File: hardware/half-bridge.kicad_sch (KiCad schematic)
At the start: 9 parts, among them Q3 PSMN039-100YS, Q4 PSMN039-100YS, U6 LM2104D

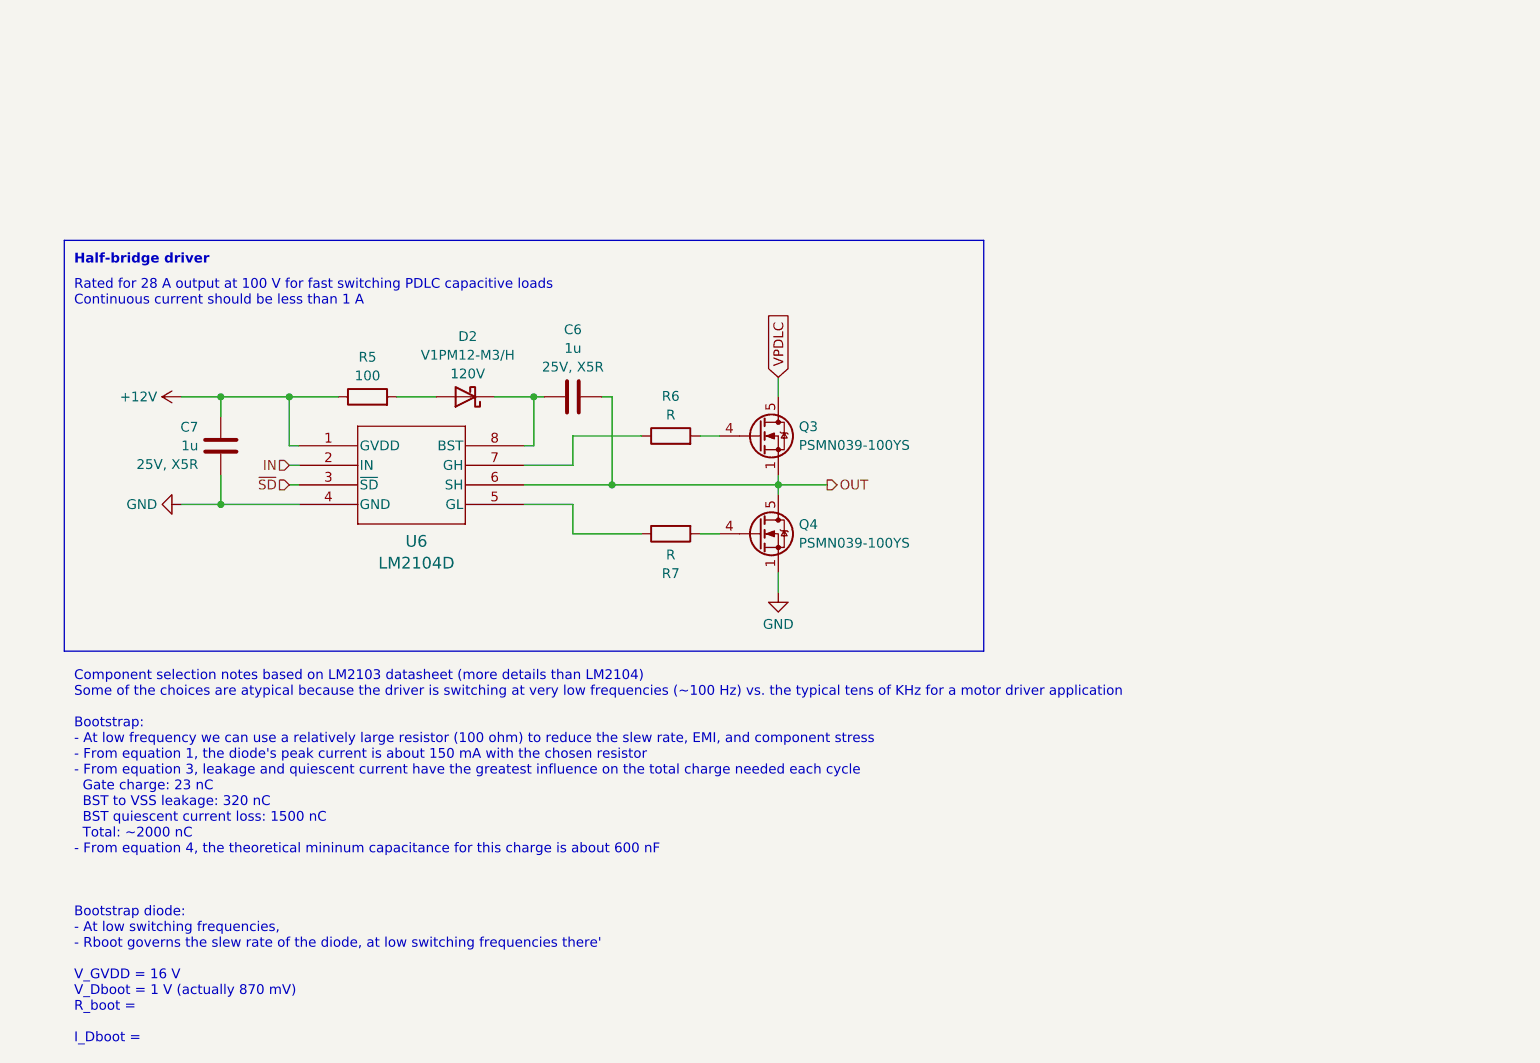
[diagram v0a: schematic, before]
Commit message: Revised layout using LM5108 and discrete FETs
LM5108 is less expensive but it requires more board area.  In lieu of
active current limiting, we rely on the LM5158 hiccup overload
protection.  The FETs are intentionally oversized to handle large
current pulses when switching the polarity of the capacitive load.

This design is complete and ready for manufacture.
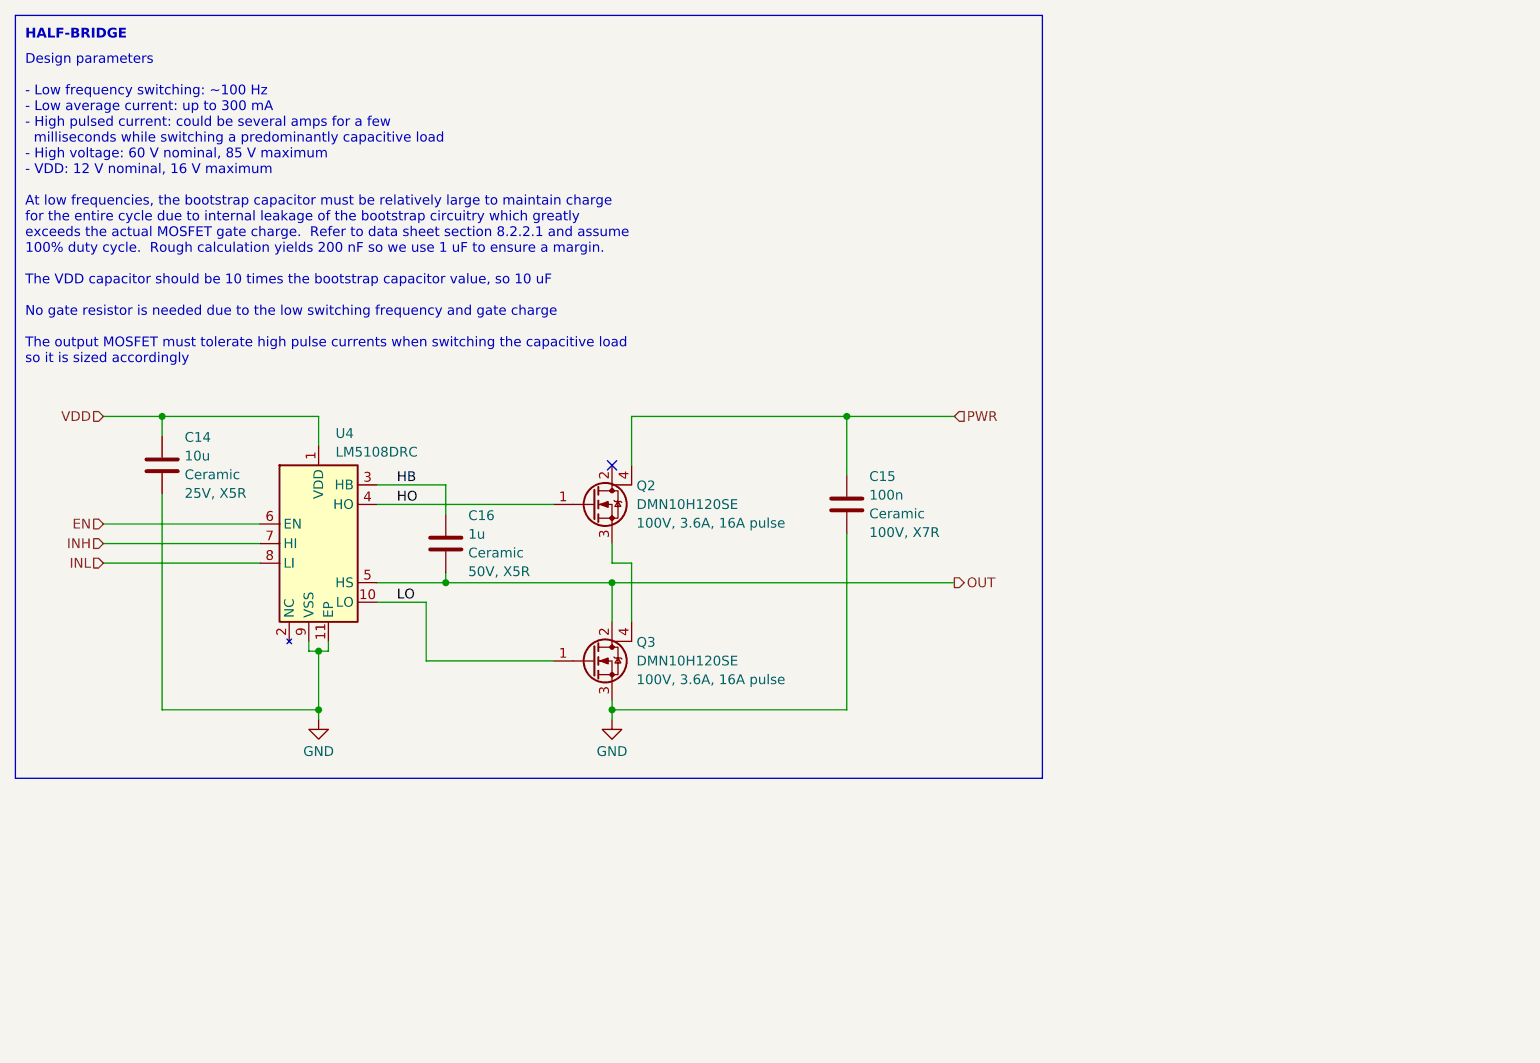
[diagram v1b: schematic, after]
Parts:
- removed C6: 1u, symbol Device:C
- removed C7: 1u, Capacitor_SMD:C_0603_1608Metric, symbol Device:C
- removed D2: V1PM12-M3/H, symbol Device:D_Schottky
- removed Q3, Q4: PSMN039-100YS, Package_TO_SOT_SMD:LFPAK56, symbol Transistor_FET:PSMN5R2-60YL
- removed R5: 100, symbol Device:R
- removed R6, R7: R, symbol Device:R
- removed U6: LM2104D, Package_SO:SOIC-8_3.9x4.9mm_P1.27mm, symbol LM2104D:LM2104D
- added C14: 10u, Capacitor_SMD:C_0603_1608Metric, symbol Device:C
- added C15: 100n, Capacitor_SMD:C_0805_2012Metric, symbol Device:C
- added C16: 1u, Capacitor_SMD:C_0603_1608Metric, symbol Device:C
- added Q2, Q3: DMN10H120SE, Package_TO_SOT_SMD:SOT-223, symbol Device:Q_NMOS_GDSD
- added U4: LM5108DRC, Package_SON:VSON-10-1EP_3x3mm_P0.5mm_EP1.65x2.4mm, symbol LM5108:LM5108DRC
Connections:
- net GND: now also C14.2, C15.2, Q3.3 (S), U4.11 (EP), U4.9 (VSS)
- net OUT: now also C16.2, Q3.2 (D), U4.5 (HS)
- new net: Q2.3 (S), Q3.4 (D)
- new net EN: U4.6 (EN)
- new net HB: C16.1, U4.3 (HB)
- new net HO: Q2.1 (G), U4.4 (HO)
- new net INH: U4.7 (HI)
- new net INL: U4.8 (LI)
- new net LO: Q3.1 (G), U4.10 (LO)
- new net PWR: C15.1, Q2.4 (D)
- new net VDD: C14.1, U4.1 (VDD)
- no-connect marks 0 -> 1
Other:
- note added: "Design parameters - Low frequency switching: ~100 Hz - Low average current: up to 300 mA - High pulsed current: could be several amps for a few milliseconds while switching a predominantly capacitive load - High voltage: 60 V nominal, 85 V maximum - VDD: 12 V nominal, 16 V maximum At low frequencies, the bootstrap capacitor must be relatively large to maintain charge for the entire cycle due to i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"
- note added: "HALF-BRIDGE"
- note removed: "Component selection notes based on LM2103 datasheet (more details than LM2104) Some of the choices are atypical because the driver is switching at very low frequencies (~100 Hz) vs. the typical tens of KHz for a motor driver application Bootstrap: - At low frequency we can use a relatively large resistor (100 ohm) to reduce the slew rate, EMI, and component stress - From equation 1, the diode's p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"
- note removed: "Half-bridge driver"
- note removed: "Rated for 28 A output at 100 V for fast switching PDLC capacitive loads Continuous current should be less than 1 A"
- title: (none) -> PDLC Driver Half Bridge
